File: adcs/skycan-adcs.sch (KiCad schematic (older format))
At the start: 33 parts, among them J1 DF9_25P_1V_PLUG, J2 DF9_25P_1V_SOCKET, J3 DF9_25P_1V_PLUG, J4 DF9_25P_1V_SOCKET

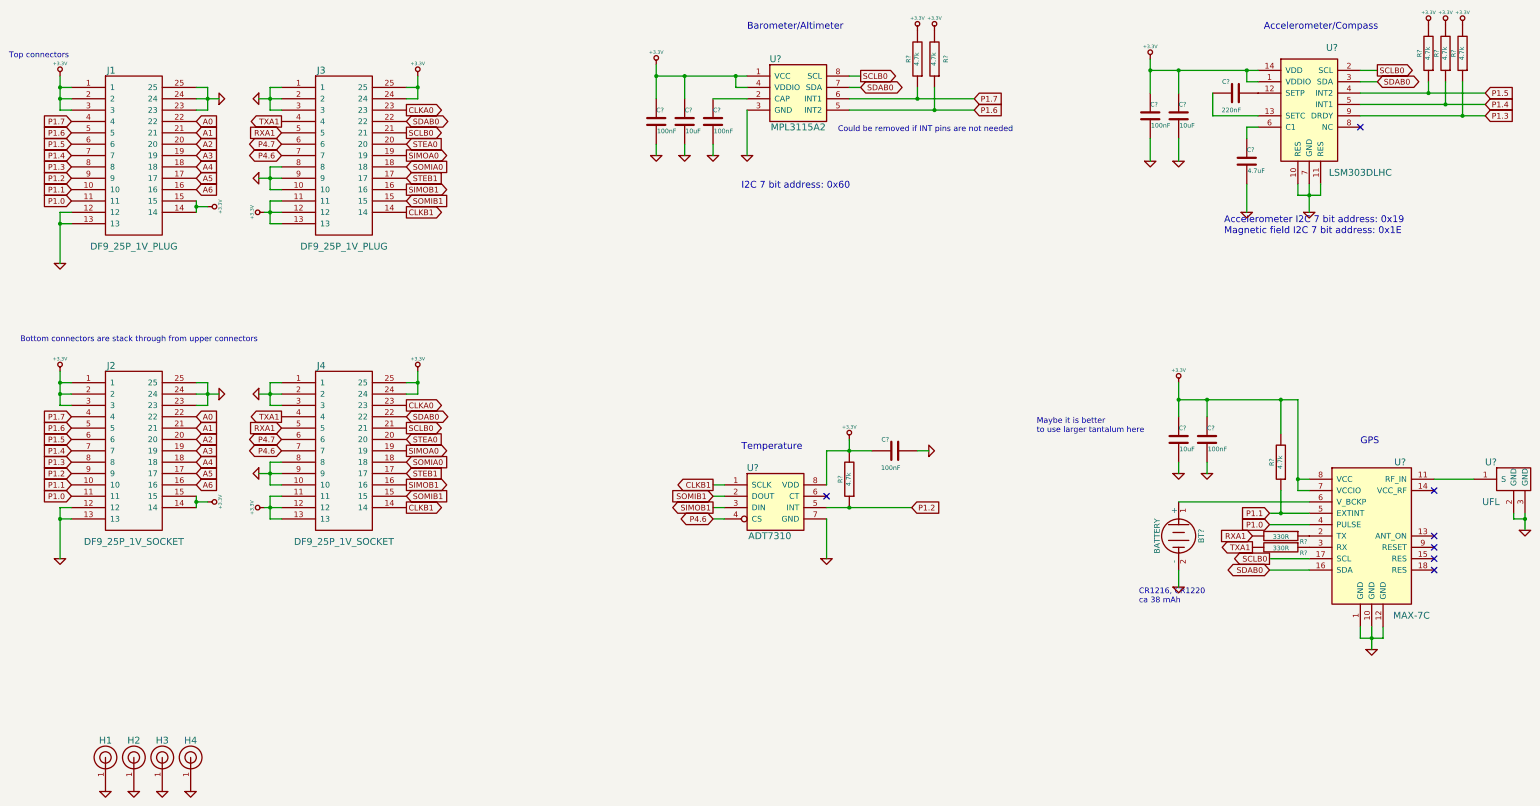
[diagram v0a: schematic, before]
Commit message: Added footprints to ADCS cmp. Save all.
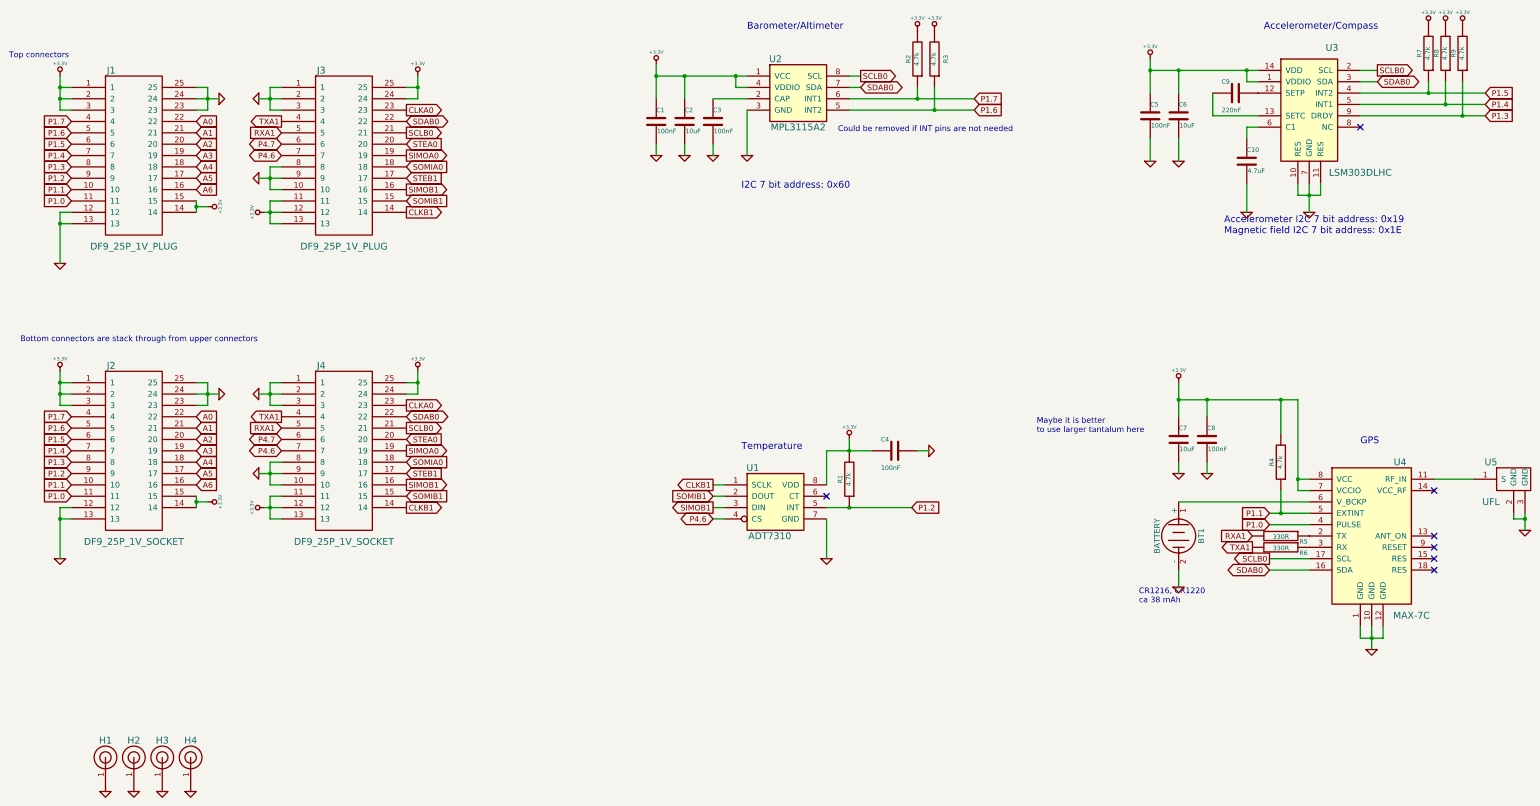
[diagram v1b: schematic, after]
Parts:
- BT1: renamed from BT?; Farnell http://ee.farnell.com/keystone/3001/retainer-coin-cell-12mm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 -> 908642
- gave numbers to parts that had none: 24

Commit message: adcs routing inprogress
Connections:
- net P1.0: now also R4.1, U4.5 (EXTINT); no longer U4.4 (PULSE)
- net P1.1: now also U4.4 (PULSE); no longer R4.1, U4.5 (EXTINT)
- net P1.2: now also R9.1, U3.9 (DRDY); no longer R1.1, U1.5 (INT)
- net P1.3: now also R1.1, U1.5 (INT); no longer R9.1, U3.9 (DRDY)
- net P1.6: now also R2.1, U2.6 (INT1); no longer R3.1, U2.5 (INT2)
- net P1.7: now also R3.1, U2.5 (INT2); no longer R2.1, U2.6 (INT1)

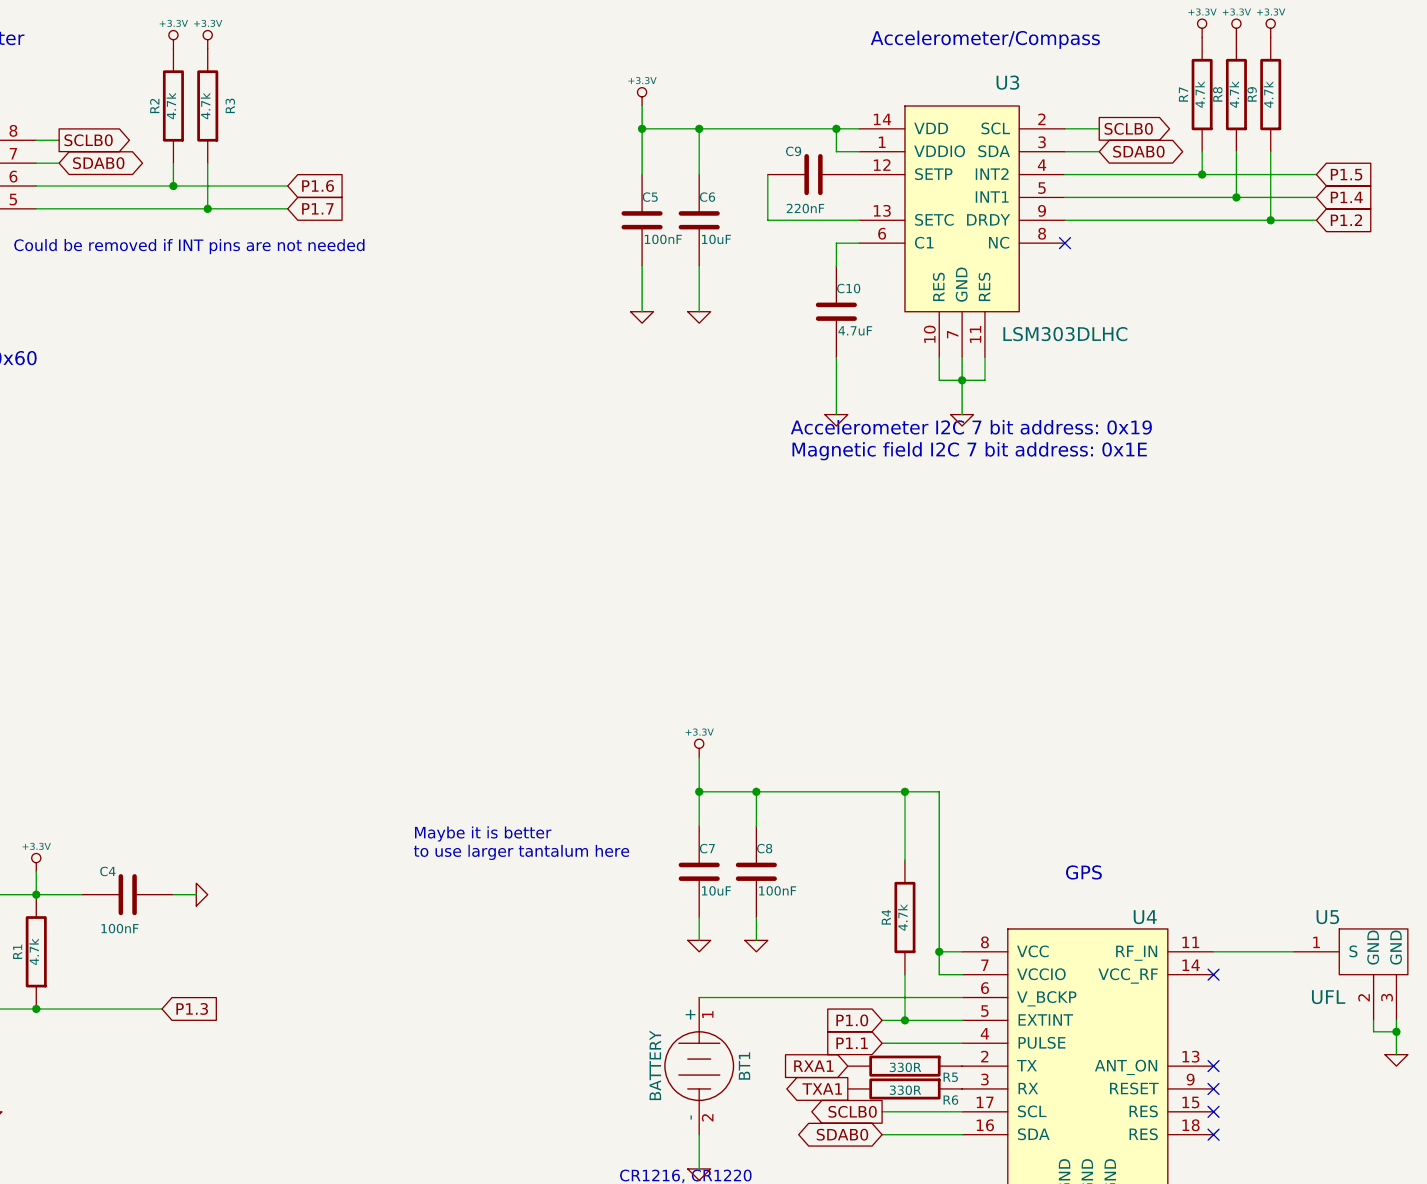
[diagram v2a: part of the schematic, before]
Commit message: signals routed
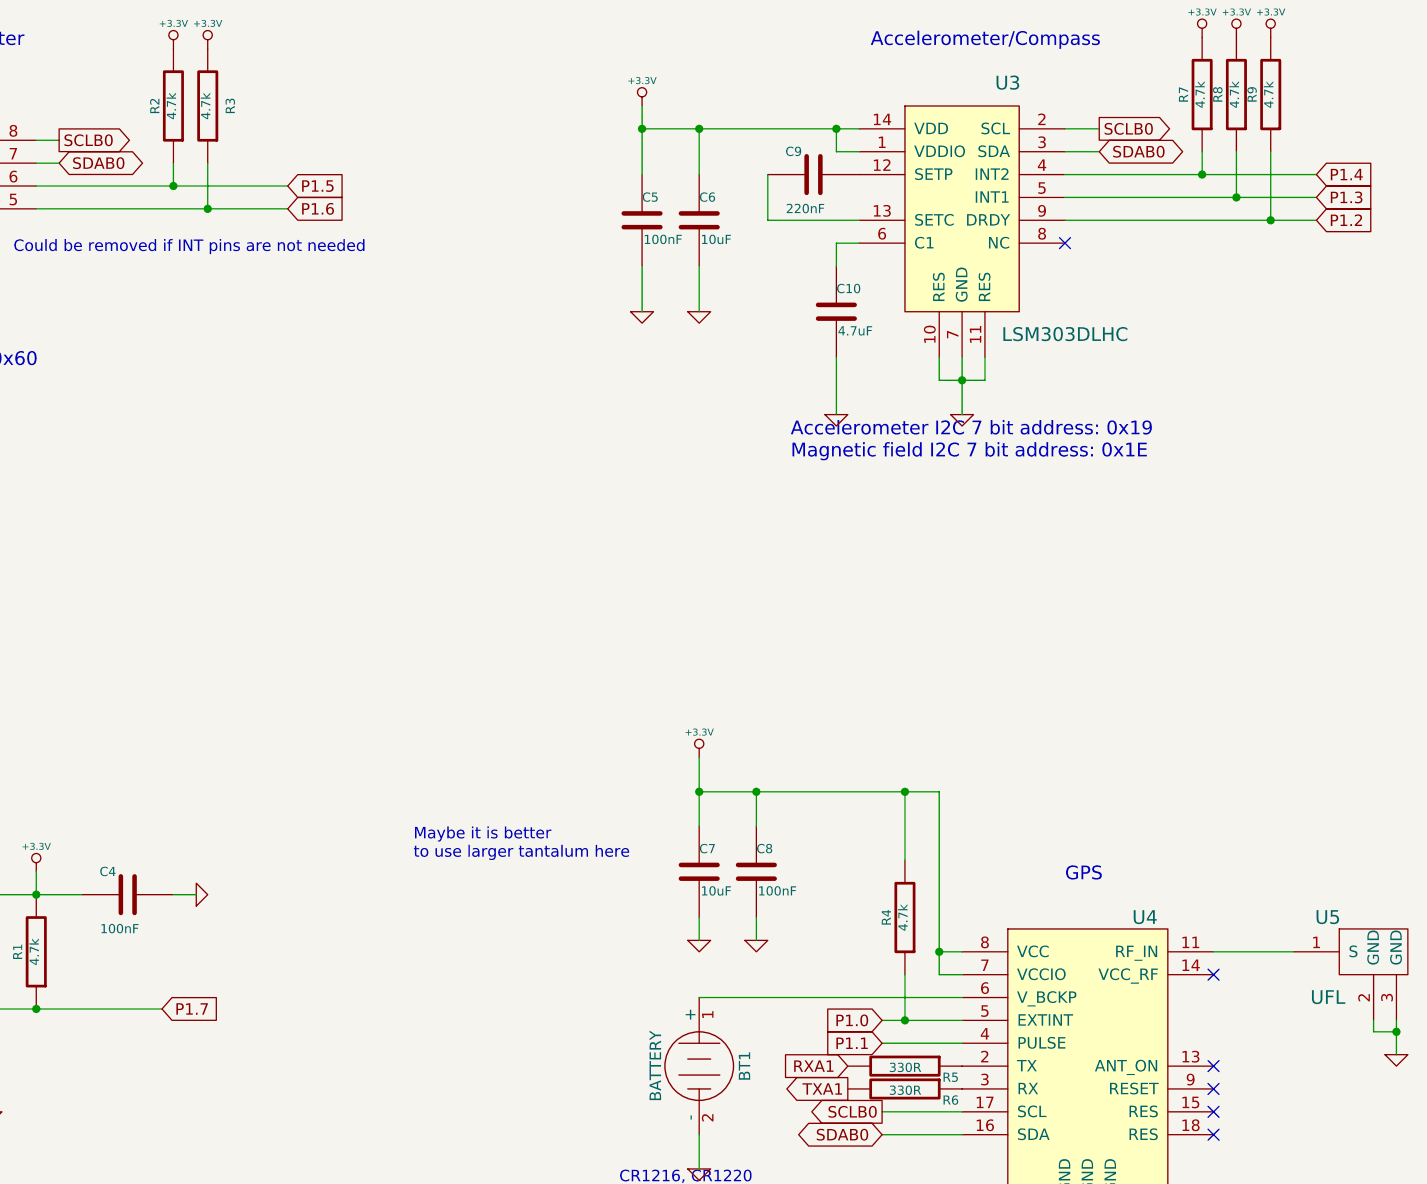
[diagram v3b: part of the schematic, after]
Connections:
- net P1.3: now also R8.1, U3.5 (INT1); no longer R1.1, U1.5 (INT)
- net P1.4: now also R7.1, U3.4 (INT2); no longer R8.1, U3.5 (INT1)
- net P1.5: now also R2.1, U2.6 (INT1); no longer R7.1, U3.4 (INT2)
- net P1.6: now also R3.1, U2.5 (INT2); no longer R2.1, U2.6 (INT1)
- net P1.7: now also R1.1, U1.5 (INT); no longer R3.1, U2.5 (INT2)
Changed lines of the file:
@@
 $EndComp
 Text GLabel 10150 2950 2    50   Input ~ 0
+P1.5
+Text GLabel 10150 3050 2    50   Input ~ 0
 P1.6
-Text GLabel 10150 3050 2    50   Input ~ 0
-P1.7
 Text Notes 8950 3250 0    50   ~ 0
 Could be removed if INT pins are not needed
@@
 Accelerometer I2C 7 bit address: 0x19\nMagnetic field I2C 7 bit address: 0x1E
 Text GLabel 14650 2900 2    50   Input ~ 0
-P1.5
+P1.4
 Text GLabel 14650 3000 2    50   Input ~ 0
-P1.4
+P1.3
 Text GLabel 14650 3100 2    50   Input ~ 0
 P1.2
@@
 $EndComp
 Text GLabel 9600 6550 2    50   Input ~ 0
-P1.3
+P1.7
 NoConn ~ 8850 6450
 Text Notes 13550 6000 0    60   ~ 0
